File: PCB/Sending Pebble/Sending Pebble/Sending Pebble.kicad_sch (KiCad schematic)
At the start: 46 parts, among them J1 USB_C_Receptacle_USB2.0_16P, J2 Conn_01x02_Socket, J3 Conn_Coaxial, J4 Conn_Coaxial, J5 Conn_01x02_Socket, Q1 IRLML0030, SW2 RESET, SW3 BOOT, U1 LoRa-E5, U3 MAX-M10S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

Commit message: Finished Footprint Assignment
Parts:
- BT1: footprint (none) -> Battery:BatteryHolder_Seiko_MS621F
- C1, C10, C2, C3, C4, C5, C6, C7, C8, C9: footprint (none) -> Capacitor_SMD:C_0603_1608Metric
- C11, C12: footprint Capacitor_SMD:C_1206_3216Metric_Pad1.33x1.80mm_HandSolder -> Capacitor_SMD:C_0603_1608Metric
- D1: footprint (none) -> Diode_SMD:D_SOD-123
- D2: footprint (none) -> LED_SMD:LED_0603_1608Metric
- J2: footprint (none) -> Connector_JST:JST_PH_S2B-PH-SM4-TB_1x02-1MP_P2.00mm_Horizontal
- J3: value Conn_Coaxial -> u.Fl; footprint (none) -> Connector_Coaxial:U.FL_Hirose_U.FL-R-SMT-1_Vertical
- J4: value Conn_Coaxial -> SMA; footprint (none) -> Connector_Coaxial:SMA_Amphenol_132289_EdgeMount
- J5: footprint (none) -> Connector_PinSocket_2.54mm:PinSocket_1x02_P2.54mm_Vertical
- R1, R10, R13, R14, R2, R3, R4, R5, R6, R7, R8, R9: footprint (none) -> Resistor_SMD:R_0603_1608Metric
- R11, R12: footprint Resistor_SMD:R_1206_3216Metric_Pad1.30x1.75mm_HandSolder -> Resistor_SMD:R_0603_1608Metric
- SW2, SW3: footprint PTS526_SM15_SMTR2_LFS:SON4_PTS526 SM15 SMTR2 LFS_CNK -> Button_Switch_SMD:SW_SPST_PTS810
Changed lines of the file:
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@@
 			)
 		)
-		(property "Footprint" ""
+		(property "Footprint" "Resistor_SMD:R_0603_1608Metric"
 			(at 62.23 105.918 90)
 			(effects
@@
 			)
 		)
-		(property "Footprint" "Resistor_SMD:R_1206_3216Metric_Pad1.30x1.75mm_HandSolder"
+		(property "Footprint" "Resistor_SMD:R_0603_1608Metric"
 			(at 41.91 170.688 90)
 			(effects
@@
 			)
 		)
-		(property "Footprint" ""
+		(property "Footprint" "Resistor_SMD:R_0603_1608Metric"
 			(at 257.81 50.038 90)
 			(effects
@@
 			)
 		)
-		(property "Footprint" ""
+		(property "Footprint" "Resistor_SMD:R_0603_1608Metric"
 			(at 111.76 184.658 90)
 			(effects
@@
 			)
 		)
-		(property "Footprint" ""
+		(property "Footprint" "Capacitor_SMD:C_0603_1608Metric"
 			(at 116.84 93.0148 0)
 			(effects
@@
 			)
 		)
-		(property "Footprint" ""
+		(property "Footprint" "Capacitor_SMD:C_0603_1608Metric"
 			(at 172.4152 101.6 0)
 			(effects
@@
 			)
 		)
-		(property "Footprint" ""
+		(property "Footprint" "Capacitor_SMD:C_0603_1608Metric"
 			(at 66.04 87.9348 0)
 			(effects
@@
 			)
 		)
-		(property "Footprint" ""
+		(property "Footprint" "Capacitor_SMD:C_0603_1608Metric"
 			(at 127 113.3348 0)
 			(effects
@@
 			)
 		)
-		(property "Footprint" ""
+		(property "Footprint" "Connector_JST:JST_PH_S2B-PH-SM4-TB_1x02-1MP_P2.00mm_Horizontal"
 			(at 260.35 43.18 0)
 			(effects
@@
 			)
 		)
-		(property "Value" "Conn_Coaxial"
+		(property "Value" "u.Fl"
 			(at 148.59 60.6424 90)
 			(effects
@@
 			)
 		)
-		(property "Footprint" ""
+		(property "Footprint" "Connector_Coaxial:U.FL_Hirose_U.FL-R-SMT-1_Vertical"
 			(at 144.78 59.69 0)
 			(effects
@@
 			)
 		)
-		(property "Footprint" ""
+		(property "Footprint" "Resistor_SMD:R_0603_1608Metric"
 			(at 62.23 100.838 90)
 			(effects
@@
 			)
 		)
-		(property "Footprint" ""
+		(property "Footprint" "Resistor_SMD:R_0603_1608Metric"
 			(at 257.81 56.642 90)
 			(effects
@@
 			)
 		)
-		(property "Footprint" ""
+		(property "Footprint" "Capacitor_SMD:C_0603_1608Metric"
 			(at 213.0552 149.86 0)
 			(effects
@@
 			)
 		)
-		(property "Footprint" "Resistor_SMD:R_1206_3216Metric_Pad1.30x1.75mm_HandSolder"
+		(property "Footprint" "Resistor_SMD:R_0603_1608Metric"
 			(at 163.068 128.27 90)
 			(effects
@@
 			)
 		)
-		(property "Footprint" "Capacitor_SMD:C_1206_3216Metric_Pad1.33x1.80mm_HandSolder"
+		(property "Footprint" "Capacitor_SMD:C_0603_1608Metric"
 			(at 175.26 139.3952 0)
 			(effects
@@
 			)
 		)
-		(property "Footprint" "Capacitor_SMD:C_1206_3216Metric_Pad1.33x1.80mm_HandSolder"
+		(property "Footprint" "Capacitor_SMD:C_0603_1608Metric"
 			(at 45.72 174.9552 0)
 			(effects
@@
 			)
 		)
-		(property "Footprint" ""
+		(property "Footprint" "Capacitor_SMD:C_0603_1608Metric"
 			(at 34.29 35.8648 0)
 			(effects
@@
 			)
 		)
-		(property "Footprint" ""
+		(property "Footprint" "Capacitor_SMD:C_0603_1608Metric"
 			(at 270.2052 135.89 0)
 			(effects
@@
 			)
 		)
-		(property "Footprint" ""
+		(property "Footprint" "Resistor_SMD:R_0603_1608Metric"
 			(at 224.79 55.118 90)
 			(effects
@@
 			)
 		)
-		(property "Footprint" ""
+		(property "Footprint" "Connector_PinSocket_2.54mm:PinSocket_1x02_P2.54mm_Vertical"
 			(at 195.58 88.9 0)
 			(effects
@@
 			)
 		)
-		(property "Footprint" ""
+		(property "Footprint" "Capacitor_SMD:C_0603_1608Metric"
 			(at 190.1952 101.6 0)
 			(effects
@@
 			)
 		)
-		(property "Footprint" ""
+		(property "Footprint" "LED_SMD:LED_0603_1608Metric"
 			(at 265.43 58.42 0)
 			(effects
@@
 			)
 		)
-		(property "Footprint" ""
+		(property "Footprint" "Capacitor_SMD:C_0603_1608Metric"
 			(at 168.6052 46.99 0)
 			(effects
@@
 			)
 		)
-		(property "Value" "Conn_Coaxial"
+		(property "Value" "SMA"
 			(at 82.55 54.9031 0)
 			(effects
@@
 			)
 		)
-		(property "Footprint" ""
+		(property "Footprint" "Connector_Coaxial:SMA_Amphenol_132289_EdgeMount"
 			(at 78.74 53.34 0)
 			(effects
@@
 			)
 		)
-		(property "Footprint" ""
+		(property "Footprint" "Resistor_SMD:R_0603_1608Metric"
 			(at 181.61 38.608 90)
 			(effects
@@
 			)
 		)
-		(property "Footprint" ""
+		(property "Footprint" "Resistor_SMD:R_0603_1608Metric"
 			(at 113.792 186.69 90)
 			(effects
@@
 			)
 		)
-		(property "Footprint" "PTS526_SM15_SMTR2_LFS:SON4_PTS526 SM15 SMTR2 LFS_CNK"
+		(property "Footprint" "Button_Switch_SMD:SW_SPST_PTS810"
 			(at 53.34 161.29 0)
 			(effects
@@
 			)
 		)
-		(property "Footprint" "PTS526_SM15_SMTR2_LFS:SON4_PTS526 SM15 SMTR2 LFS_CNK"
+		(property "Footprint" "Button_Switch_SMD:SW_SPST_PTS810"
 			(at 171.45 127 0)
 			(effects
@@
 			)
 		)
-		(property "Footprint" ""
+		(property "Footprint" "Resistor_SMD:R_0603_1608Metric"
 			(at 90.932 97.79 90)
 			(effects
@@
 			)
 		)
-		(property "Footprint" ""
+		(property "Footprint" "Resistor_SMD:R_0603_1608Metric"
 			(at 224.79 57.658 90)
 			(effects
@@
 			)
 		)
-		(property "Footprint" ""
+		(property "Footprint" "Resistor_SMD:R_0603_1608Metric"
 			(at 229.87 148.082 90)
 			(effects
@@
 			)
 		)
-		(property "Footprint" ""
+		(property "Footprint" "Resistor_SMD:R_0603_1608Metric"
 			(at 215.392 129.54 90)
 			(effects
@@
 			)
 		)
-		(property "Footprint" ""
+		(property "Footprint" "Capacitor_SMD:C_0603_1608Metric"
 			(at 66.04 93.0148 0)
 			(effects
@@
 			)
 		)
-		(property "Footprint" ""
+		(property "Footprint" "Battery:BatteryHolder_Seiko_MS621F"
 			(at 176.53 40.386 90)
 			(effects
@@
 			)
 		)
-		(property "Footprint" ""
+		(property "Footprint" "Diode_SMD:D_SOD-123"
 			(at 186.69 33.02 0)
 			(effects

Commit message: Started Layout, Added DRC
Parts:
- removed SW2: RESET, Button_Switch_SMD:SW_SPST_PTS810, symbol Switch:SW_MEC_5E
- removed SW3: BOOT, Button_Switch_SMD:SW_SPST_PTS810, symbol Switch:SW_MEC_5E
- added SW1: Boot, Button_Switch_SMD:SW_SPST_PTS810, symbol Switch:SW_Push
- added SW2: Reset, Button_Switch_SMD:SW_SPST_PTS810, symbol Switch:SW_Push
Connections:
- net +3.3V: now also SW1.1
- net BOOT0: now also SW1.2
- net GND: now also SW2.2
- net PB6/TX: no longer U1.9 (PB7)
- net PB7/RX: now also U1.9 (PB7)
- net RST: now also SW2.1
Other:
- note added: "Wio E5"
- title: (none) -> Sending Pebble v1
- moved on the sheet: BT1, BZ1, C1, C10, C11, C12, C3, C4, C5, C6, C7, C8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

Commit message: Power Circuitry almost finished
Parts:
- added R15: 10k, Resistor_SMD:R_0603_1608Metric, symbol Device:R
- added R16: 36k, Resistor_SMD:R_0603_1608Metric, symbol Device:R
- R10: value 3k -> 1.27k
- R9: value 3k -> 1.1k
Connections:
- net +3.3V: now also C4.1, U5.3 (OUT); no longer J5.2 (Pin_2)
- net GND: now also J2.1 (Pin_1), R10.1, R9.1, U7.6 (EN1), R16.2; no longer J2.2 (Pin_2), U7.5 (EN2)
- net VBAT: now also J5.1 (Pin_1); no longer C3.1, U5.1 (IN)
- net VBUS: now also U7.5 (EN2); no longer U7.6 (EN1)
- net ADC: now reaches U1.26 (PB14)
- net ADC: now also R15.2, R16.1
- net at U7.2 (BAT), U7.3 (BAT): now also J2.2 (Pin_2), R15.1; no longer J2.1 (Pin_1)
- new net: C3.1, J5.2 (Pin_2), U5.1 (IN)
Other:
- moved on the sheet: C3, C4, J2, J5, U5

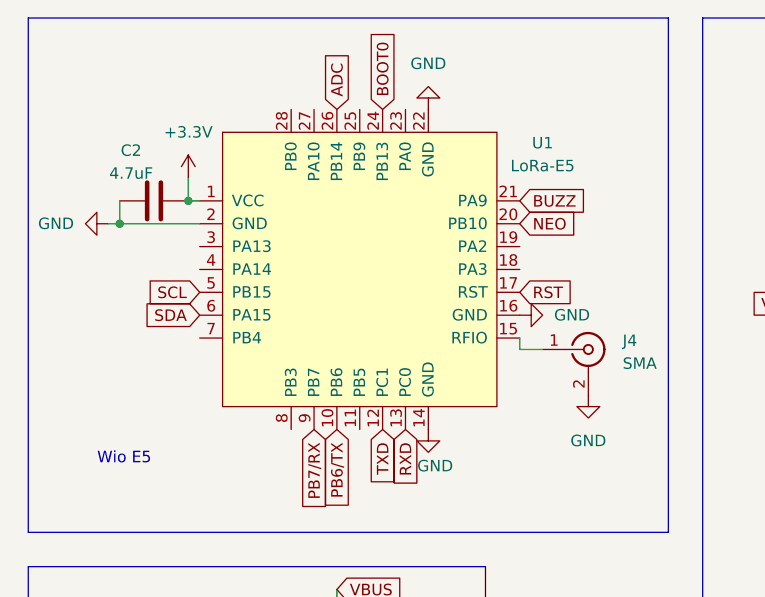
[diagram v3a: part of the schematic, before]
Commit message: Finalized form factor, added coplanar waveguides for feedlines and placed all components on board
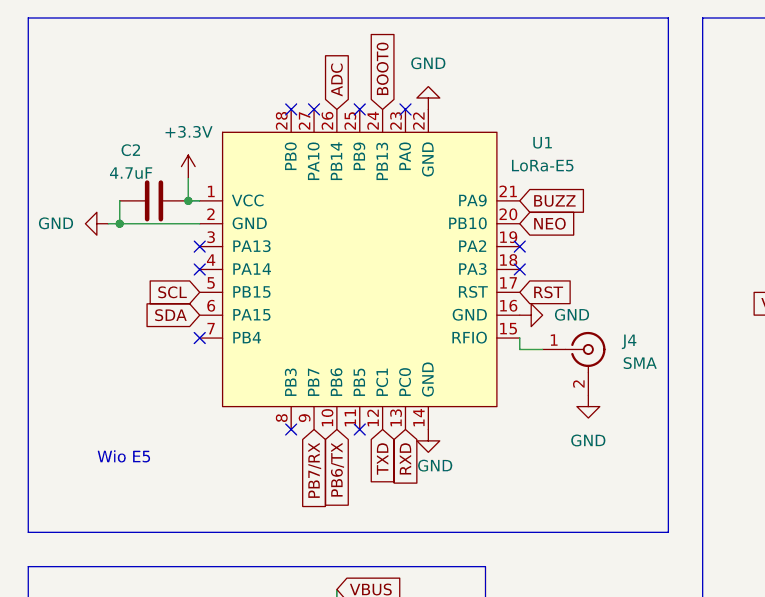
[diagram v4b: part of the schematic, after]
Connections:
- no-connect marks 25 -> 36
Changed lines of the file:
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@@
+	)
+	(no_connect
+		(at 71.12 44.45)
 	)
 	(no_connect
@@
 	)
 	(no_connect
+		(at 35.56 52.07)
+	)
+	(no_connect
 		(at 168.91 55.88)
 	)
 	(no_connect
+		(at 35.56 41.91)
+	)
+	(no_connect
+		(at 53.34 26.67)
+	)
+	(no_connect
 		(at 129.54 58.42)
 	)
 	(no_connect
+		(at 48.26 26.67)
+	)
+	(no_connect
 		(at 163.83 25.4)
 	)
@@
 	)
 	(no_connect
+		(at 58.42 26.67)
+	)
+	(no_connect
 		(at 179.07 25.4)
 	)
 	(no_connect
+		(at 53.34 62.23)
+	)
+	(no_connect
 		(at 129.54 45.72)
 	)
@@
 	)
 	(no_connect
+		(at 71.12 41.91)
+	)
+	(no_connect
 		(at 166.37 25.4)
 	)
@@
 	)
 	(no_connect
+		(at 45.72 26.67)
+	)
+	(no_connect
 		(at 129.54 60.96)
 	)
 	(no_connect
+		(at 45.72 62.23)
+	)
+	(no_connect
+		(at 35.56 44.45)
+	)
+	(no_connect
 		(at 129.54 40.64)
 	)
@@
 			)
 		)
+	)
+	(netclass_flag ""
+		(length 2.54)
+		(shape round)
+		(at 72.39 53.34 180)
+		(fields_autoplaced yes)
+		(effects
+			(font
+				(size 1.27 1.27)
+			)
+			(justify right bottom)
+		)
+		(property "Netclass" "915MHz"
+			(at 73.0885 55.88 0)
+			(effects
+				(font
+					(size 1.27 1.27)
+				)
+				(justify left)
+			)
+		)
+		(property "Component Class" ""
+			(at -312.42 -1.27 0)
+			(effects
+				(font
+					(size 1.27 1.27)
+					(italic yes)
+				)
+			)
+		)
+	)
+	(netclass_flag ""
+		(length 2.54)
+		(shape round)
+		(at 176.53 57.15 270)
+		(fields_autoplaced yes)
+		(effects
+			(font
+				(size 1.27 1.27)
+			)
+			(justify right bottom)
+		)
+		(property "Netclass" "GPS"
+			(at 179.07 56.4515 90)
+			(effects
+				(font
+					(size 1.27 1.27)
+				)
+				(justify left)
+			)
+		)
+		(property "Component Class" ""
+			(at -165.1 -17.78 0)
+			(effects
+				(font
+					(size 1.27 1.27)
+					(italic yes)
+				)
+			)
+		)

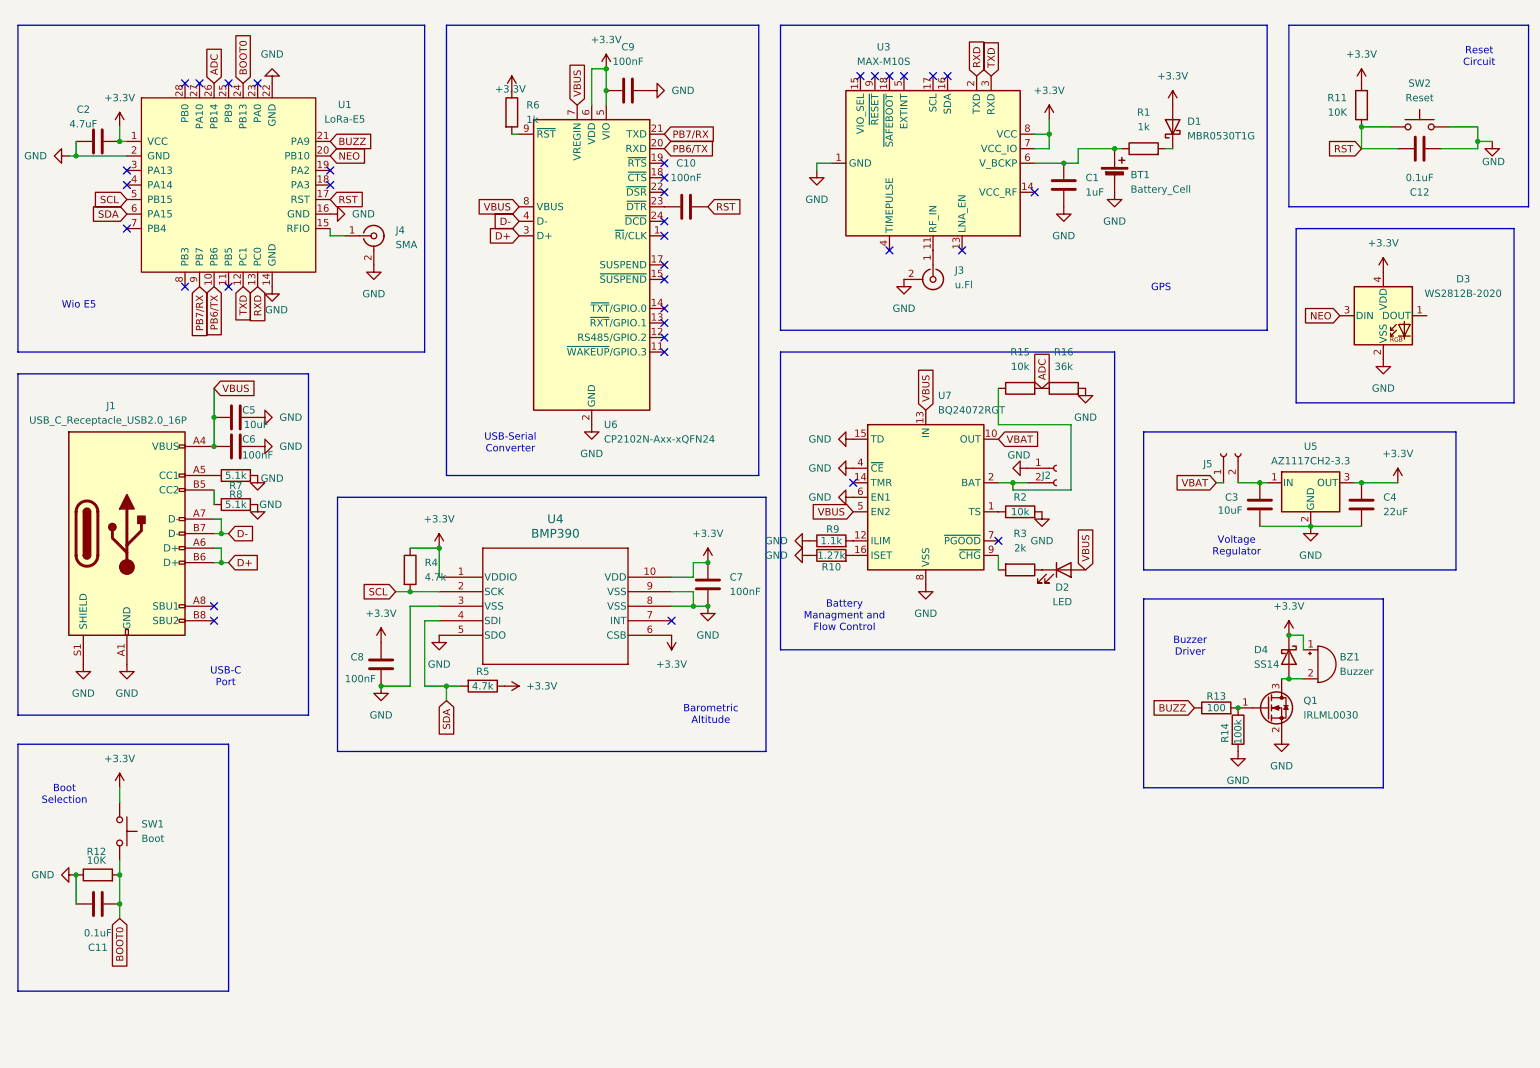
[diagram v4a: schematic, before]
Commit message: Fixed VREG type, more routing
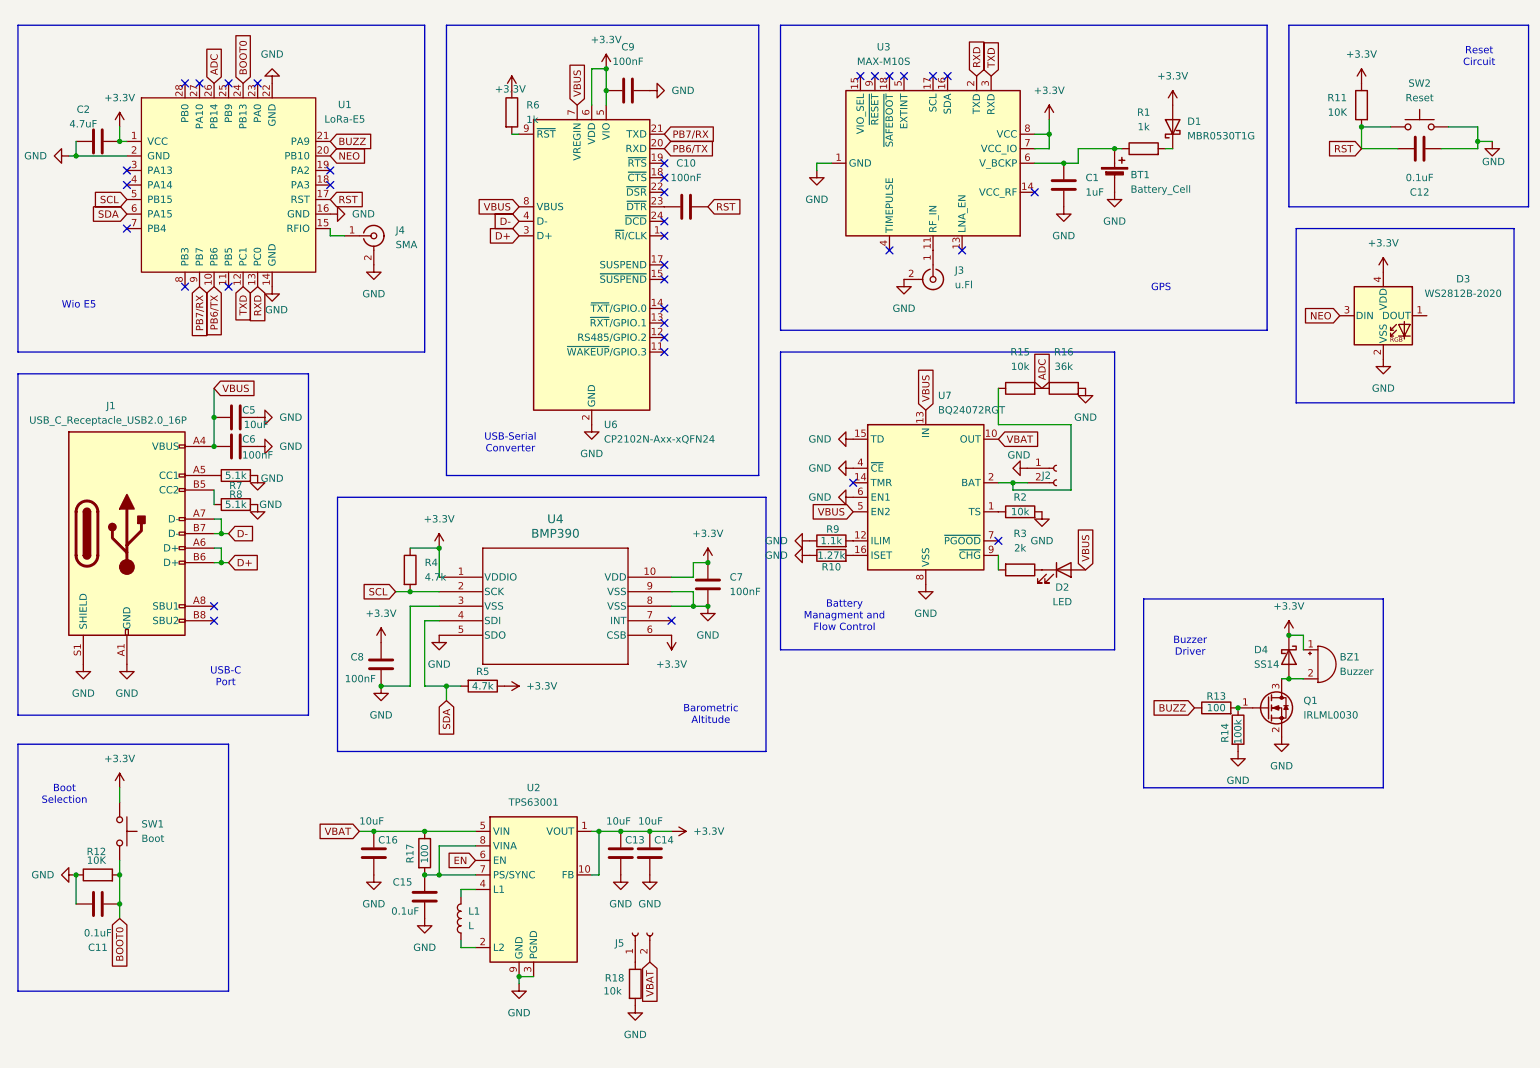
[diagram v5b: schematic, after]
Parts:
- removed C3: 10uF, Capacitor_SMD:C_0603_1608Metric, symbol Device:C
- removed C4: 22uF, Capacitor_SMD:C_0603_1608Metric, symbol Device:C
- removed U5: AZ1117CH2-3.3, Package_TO_SOT_SMD:SOT-223-3_TabPin2, symbol Regulator_Linear:AZ1117CH2-3.3
- added C13, C14, C16: 10uF, Capacitor_SMD:C_0603_1608Metric, symbol Device:C
- added C15: 0.1uF, Capacitor_SMD:C_0603_1608Metric, symbol Device:C
- added L1: L, LQH3NPN2R2MMEL:IND_LQH3NPN2R2MMEL, symbol Device:L
- added R17: 100, Resistor_SMD:R_0603_1608Metric, symbol Device:R
- added R18: 10k, Resistor_SMD:R_0603_1608Metric, symbol Device:R
- added U2: TPS63001, Package_SON:Texas_DRC0010J_ThermalVias, symbol Regulator_Switching:TPS63001
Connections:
- net +3.3V: now also C13.1, C14.1, U2.1 (VOUT), U2.10 (FB)
- net GND: now also C13.2, C14.2, C15.2, C16.2, R18.2, U2.11 (PGND), U2.3 (PGND), U2.9 (GND)
- net VBAT: now also J5.2 (Pin_2), C16.1, R17.1, U2.5 (VIN); no longer J5.1 (Pin_1)
- new net: L1.1, U2.2 (L2)
- new net: L1.2, U2.4 (L1)
- new net: C15.1, R17.2, U2.7 (PS/SYNC), U2.8 (VINA)
- new net: J5.1 (Pin_1), R18.1
- new net EN: U2.6 (EN)
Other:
- note removed: "Voltage Regulator"
- moved on the sheet: J5

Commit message: More routing, added FC connection
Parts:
- added J5: Conn_01x03_Socket, symbol Connector:Conn_01x03_Socket
- renumbered SW1 to BOOT0, J5 to PWR0, SW2 to RESET0
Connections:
- net EN: now also PWR0.1 (Pin_1), R18.1
- net GND: now also J5.1 (Pin_1)
- net FC-TX: now reaches U1.3 (PA13)
- net FC-TX: now also J5.2 (Pin_2)
- net FC-RX: now reaches U1.4 (PA14)
- net FC-RX: now also J5.3 (Pin_3)
- no-connect marks 36 -> 34
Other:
- note added: "FC Connection"
